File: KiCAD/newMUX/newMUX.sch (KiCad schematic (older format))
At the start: 43 parts, among them J1 Conn_01x14, J2 Conn_02x06_Odd_Even, J3 Conn_02x06_Odd_Even, J4 Conn_01x14, U1 ASSR-1611, U10 ASSR-1611, U11 ASSR-1611, U12 ASSR-1611, U13 ASSR-1611, U14 ASSR-1611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

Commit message: MIT redesign in progress
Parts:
- removed R2: 500K, Resistor_SMD:R_1206_3216Metric, symbol Device:R
- L1: value GREY@CHRISTOFORO.NET -> grey@mutovis.com; footprint myParts:logo -> logo:text; symbol myParts:GREY@CHRISTOFORO.NET -> logo:logo_text
- TP1: symbol Connector_Specialized:Test_Point -> Connector:TestPoint
- U22: symbol microchip:MCP23S17 -> Interface_Expansion:MCP23S17_SP
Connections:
- net labels added: RSense
- net labels removed: RH, RL
- wire segments 229 -> 223
- no-connect marks 28 -> 29
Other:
- moved on the sheet: C1, J2, J3, R1, R3

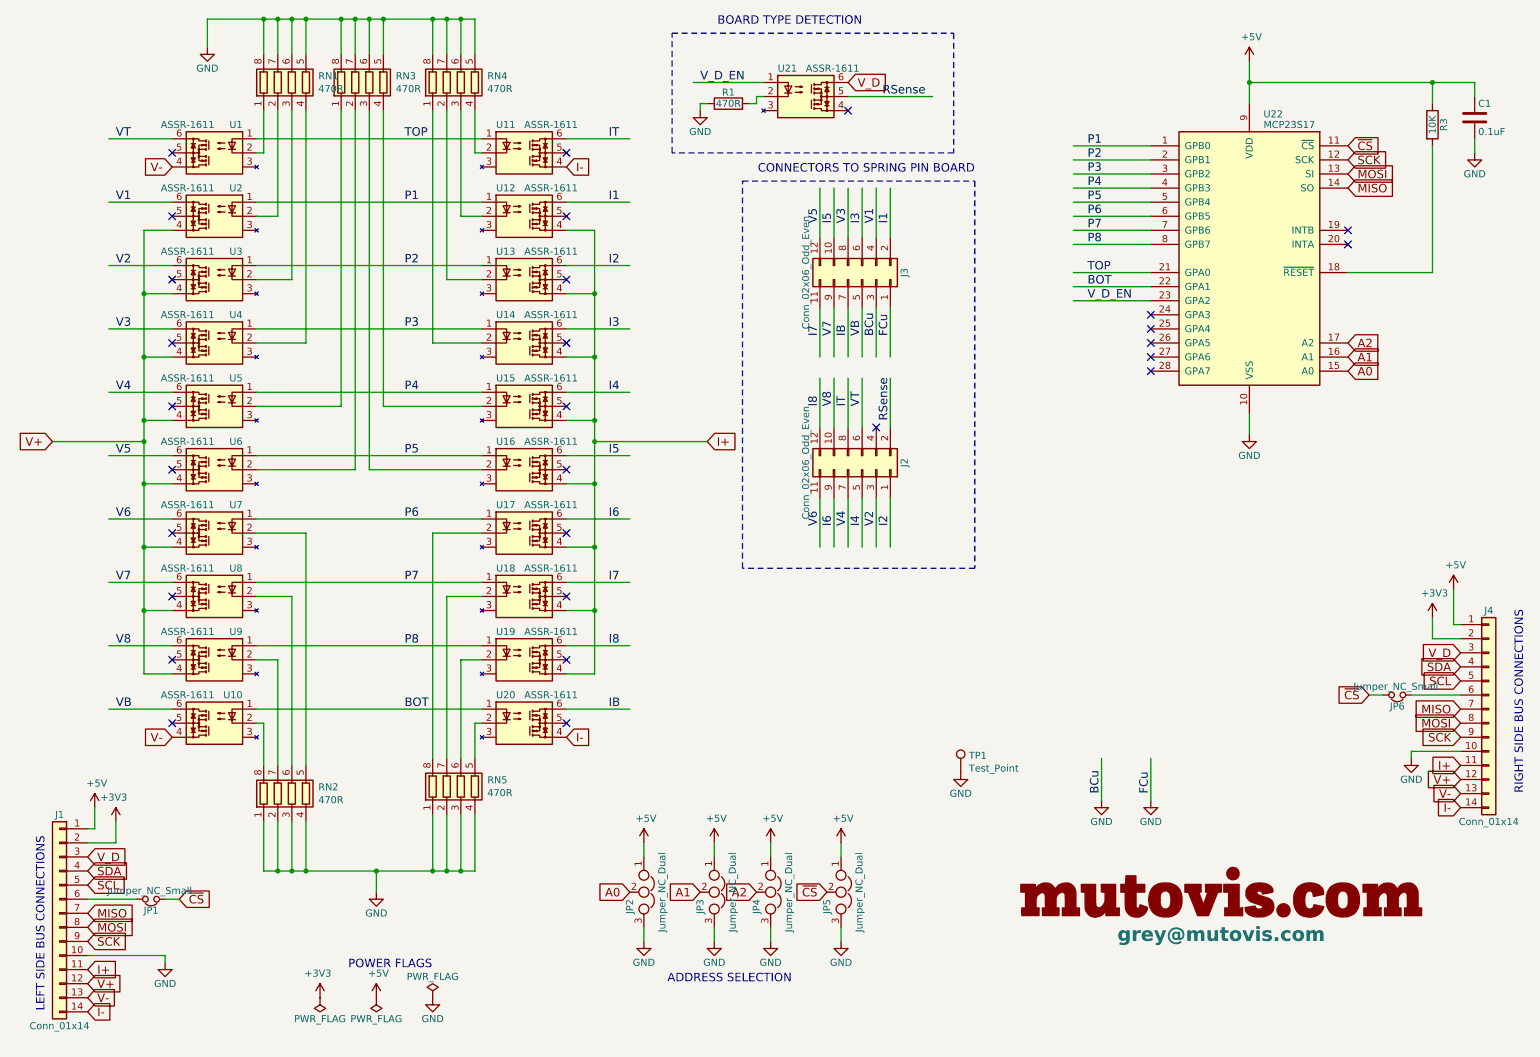
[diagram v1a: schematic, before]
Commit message: new base1x layed out, mux updated and re-layed out
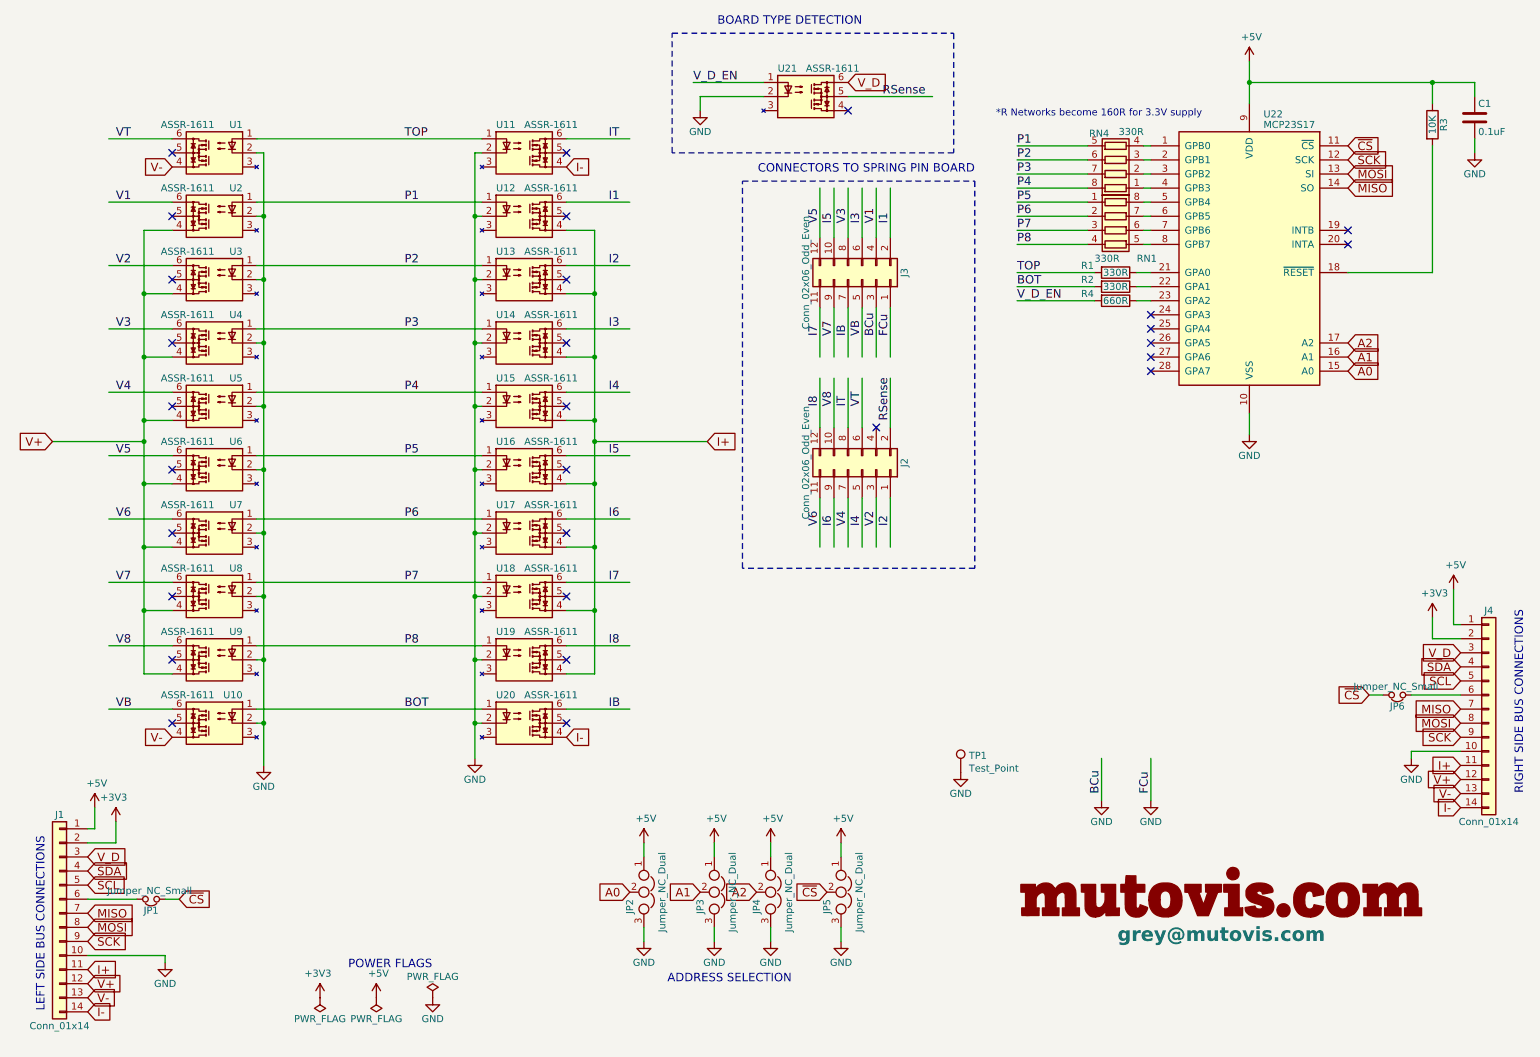
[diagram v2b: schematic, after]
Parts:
- removed RN2, RN3, RN5: 470R, myParts:VISHAY_CRA12E, symbol Device:R_Pack04
- added R2: 330R, Resistor_SMD:R_1206_3216Metric_Pad1.42x1.75mm_HandSolder, symbol Device:R
- added R4: 660R, Resistor_SMD:R_1206_3216Metric_Pad1.42x1.75mm_HandSolder, symbol Device:R
- R1: value 470R -> 330R; footprint Resistor_SMD:R_1206_3216Metric -> Resistor_SMD:R_1206_3216Metric_Pad1.42x1.75mm_HandSolder; farnellCode 2073783 -> 2073607
- R3: footprint Resistor_SMD:R_1206_3216Metric -> Resistor_SMD:R_1206_3216Metric_Pad1.42x1.75mm_HandSolder
- RN1, RN4: value 470R -> 330R; footprint myParts:VISHAY_CRA12E -> Resistor_SMD:R_Array_Convex_4x1206
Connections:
- wire segments 223 -> 189
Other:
- note added: "*R Networks become 160R for 3.3V supply"
- moved on the sheet: RN4

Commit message: update holder for mit
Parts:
- C1: farnellCode 1759143 -> 1759312
- R3: farnellCode 2073607 -> 2826357
- R4: value 660R -> 680R; farnellCode 2073607 -> 2694489
- RN1, RN4: farnellCode 2352777 -> 9234489
- TP1: farnell code (none) -> 2293786
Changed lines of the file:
@@
 F 2 "Capacitor_SMD:C_0805_2012Metric" H 10838 1100 50  0001 C CNN
 F 3 "" H 10800 1250 50  0001 C CNN
-F 4 "1759143" H -100 300 50  0001 C CNN "farnellCode"
+F 4 "1759312" H -100 300 50  0001 C CNN "farnellCode"
 	1    10800 1250
 	1    0    0    -1
@@
 F 2 "Resistor_SMD:R_1206_3216Metric_Pad1.42x1.75mm_HandSolder" V 10430 1300 50  0001 C CNN
 F 3 "" H 10500 1300 50  0000 C CNN
-F 4 "2073607" H -100 300 50  0001 C CNN "farnellCode"
+F 4 "2826357" H -100 300 50  0001 C CNN "farnellCode"
 	1    10500 1300
 	1    0    0    -1
@@
 F 2 "Resistor_SMD:R_Array_Convex_4x1206" V 8525 1550 50  0001 C CNN
 F 3 "" H 8250 1550 50  0001 C CNN
-F 4 "2352777" H 8250 1550 60  0001 C CNN "farnellCode"
+F 4 "9234489" H 8250 1550 60  0001 C CNN "farnellCode"
 	1    8250 1550
 	0    -1   -1   0
@@
 F 2 "myParts:Test_Point_S1751-46R" H 7350 5900 50  0001 C CNN
 F 3 "" H 7350 5900 50  0001 C CNN
+F 4 "2293786" H 7150 5900 50  0001 C CNN "farnell code"
 	1    7150 5900
 	1    0    0    -1
@@
 F 2 "Resistor_SMD:R_Array_Convex_4x1206" V 8525 2050 50  0001 C CNN
 F 3 "" H 8250 2050 50  0001 C CNN
-F 4 "2352777" H 8250 2050 60  0001 C CNN "farnellCode"
+F 4 "9234489" H 8250 2050 60  0001 C CNN "farnellCode"
 	1    8250 2050
 	0    1    1    0
@@
 P 8250 2550
 F 0 "R4" V 8200 2350 50  0000 C CNN
-F 1 "660R" V 8250 2550 50  0000 C CNN
+F 1 "680R" V 8250 2550 50  0000 C CNN
 F 2 "Resistor_SMD:R_1206_3216Metric_Pad1.42x1.75mm_HandSolder" V 8180 2550 50  0001 C CNN
 F 3 "" H 8250 2550 50  0000 C CNN
-F 4 "2073607" H -2350 1550 50  0001 C CNN "farnellCode"
+F 4 "2694489" H -2350 1550 50  0001 C CNN "farnellCode"
 	1    8250 2550
 	0    1    1    0

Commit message: update connector components and design printed bottom header shroud
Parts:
- J2: footprint Connector_PinSocket_2.54mm:PinSocket_2x06_P2.54mm_Vertical -> myParts:ESQ-106-44-G-D-004; farnellCode 1930232 -> (none); samtec (none) -> ESQ-106-44-G-D-004
- J3: footprint Connector_PinSocket_2.54mm:PinSocket_2x06_P2.54mm_Vertical -> myParts:ESQ-106-44-G-D; FarnellPart (none) -> 1930232; farnellCode 1930232 -> (none)
- RN1, RN4: digikey (none) -> 744C083331JPCT-ND; farnellCode 9234489 -> (none)
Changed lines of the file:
@@
 F 0 "J2" H 6500 4050 50  0000 C CNN
 F 1 "Conn_02x06_Odd_Even" H 6500 3350 50  0000 C CNN
-F 2 "Connector_PinSocket_2.54mm:PinSocket_2x06_P2.54mm_Vertical" H 6450 3750 50  0001 C CNN
+F 2 "myParts:ESQ-106-44-G-D-004" H 6450 3750 50  0001 C CNN
 F 3 "" H 6450 3750 50  0001 C CNN
-F 4 "1930232" H -1400 -650 50  0001 C CNN "farnellCode"
+F 4 "ESQ-106-44-G-D-004" H -1400 -650 50  0001 C CNN "samtec"
 	1    6450 3750
 	0    1    -1   0
@@
 F 0 "J3" H 6500 2700 50  0000 C CNN
 F 1 "Conn_02x06_Odd_Even" H 6500 2000 50  0000 C CNN
-F 2 "Connector_PinSocket_2.54mm:PinSocket_2x06_P2.54mm_Vertical" H 6450 2400 50  0001 C CNN
+F 2 "myParts:ESQ-106-44-G-D" H 6450 2400 50  0001 C CNN
 F 3 "" H 6450 2400 50  0001 C CNN
-F 4 "1930232" H -1400 -650 50  0001 C CNN "farnellCode"
+F 4 "1930232" H -1400 -650 50  0001 C CNN "FarnellPart"
 	1    6450 2400
 	0    1    -1   0
@@
 F 2 "Resistor_SMD:R_Array_Convex_4x1206" V 8525 1550 50  0001 C CNN
 F 3 "" H 8250 1550 50  0001 C CNN
-F 4 "9234489" H 8250 1550 60  0001 C CNN "farnellCode"
+F 4 "744C083331JPCT-ND" H 8250 1550 60  0001 C CNN "digikey"
 	1    8250 1550
 	0    -1   -1   0
@@
 F 2 "Resistor_SMD:R_Array_Convex_4x1206" V 8525 2050 50  0001 C CNN
 F 3 "" H 8250 2050 50  0001 C CNN
-F 4 "9234489" H 8250 2050 60  0001 C CNN "farnellCode"
+F 4 "744C083331JPCT-ND" H 8250 2050 60  0001 C CNN "digikey"
 	1    8250 2050
 	0    1    1    0

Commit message: improve bottom shroud
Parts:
- C1: footprint Capacitor_SMD:C_0805_2012Metric -> Capacitor_SMD:C_1206_3216Metric_Pad1.42x1.75mm_HandSolder
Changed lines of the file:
@@
 F 0 "C1" H 10825 1350 50  0000 L CNN
 F 1 "0.1uF" H 10825 1150 50  0000 L CNN
-F 2 "Capacitor_SMD:C_0805_2012Metric" H 10838 1100 50  0001 C CNN
+F 2 "Capacitor_SMD:C_1206_3216Metric_Pad1.42x1.75mm_HandSolder" H 10838 1100 50  0001 C CNN
 F 3 "" H 10800 1250 50  0001 C CNN
 F 4 "1759312" H -100 300 50  0001 C CNN "farnellCode"
